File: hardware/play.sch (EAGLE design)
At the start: 12 parts, among them T1 BC547, T2 BC547, T3 BC547, T4 BC547

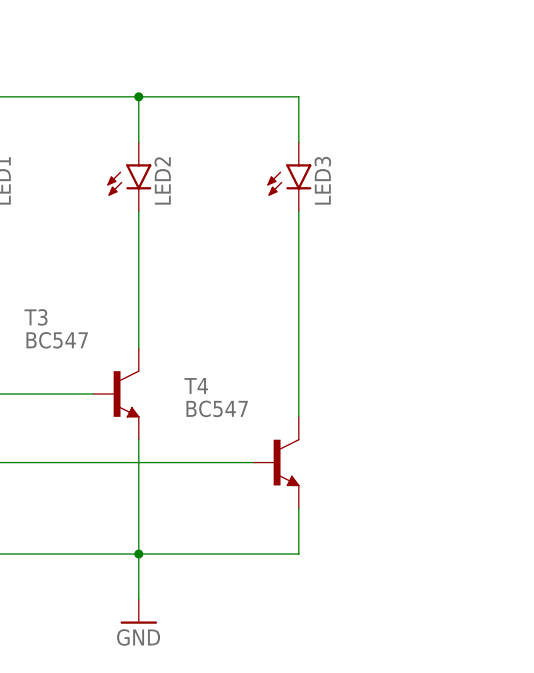
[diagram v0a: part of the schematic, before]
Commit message: Added smoothing cap on the schematic
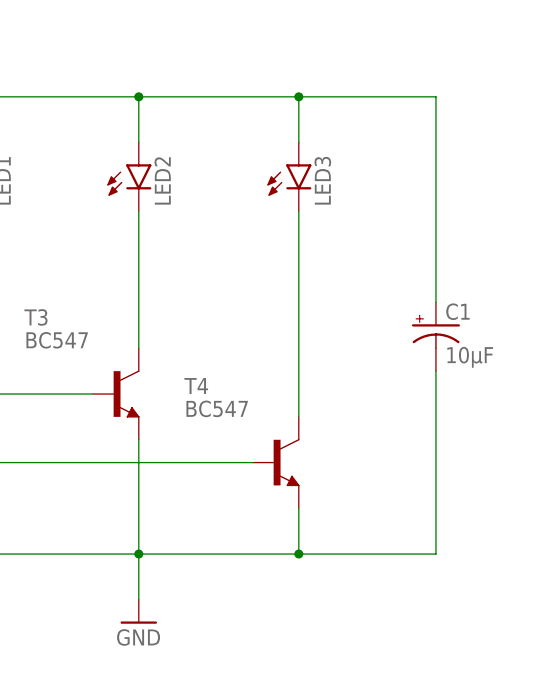
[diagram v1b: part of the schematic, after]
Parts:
- added C1: 10µF, SparkFun-Capacitors:CAP_POLPTH2
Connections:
- net GND: now also C1.-
- net VCC: now also C1.+
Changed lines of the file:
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@@
 <setting verticaltext="up"/>
 </settings>
-<grid distance="0.1" unitdist="inch" unit="inch" style="lines" multiple="1" display="yes" altdistance="0.01" altunitdist="inch" altunit="inch"/>
+<grid distance="0.1" unitdist="inch" unit="inch" style="lines" multiple="1" display="no" altdistance="0.01" altunitdist="inch" altunit="inch"/>
 <layers>
 <layer number="1" name="Top" color="4" fill="1" visible="no" active="no"/>
@@
 </part>
 <part name="S1" library="SparkFun-Electromechanical" deviceset="SWITCH-MOMENTARY-2" device="PTH"/>
+<part name="C1" library="SparkFun-Capacitors" deviceset="CAP_POL" device="PTH2" value="10µF"/>
 </parts>
 <sheets>
@@
 </instance>
 <instance part="S1" gate="G$1" x="68.58" y="33.02" rot="R270"/>
+<instance part="C1" gate="G$1" x="165.1" y="30.48"/>
 </instances>
 <busses>
@@
 <junction x="114.3" y="55.88"/>
 <junction x="132.08" y="55.88"/>
+<pinref part="C1" gate="G$1" pin="+"/>
+<wire x1="149.86" y1="55.88" x2="165.1" y2="55.88" width="0.1524" layer="91"/>
+<wire x1="165.1" y1="55.88" x2="165.1" y2="33.02" width="0.1524" layer="91"/>
+<junction x="149.86" y="55.88"/>
 </segment>
 </net>
@@
 <wire x1="68.58" y1="5.08" x2="114.3" y2="5.08" width="0.1524" layer="91"/>
 <junction x="114.3" y="5.08"/>
+<pinref part="C1" gate="G$1" pin="-"/>
+<wire x1="165.1" y1="25.4" x2="165.1" y2="5.08" width="0.1524" layer="91"/>
+<wire x1="165.1" y1="5.08" x2="149.86" y2="5.08" width="0.1524" layer="91"/>
+<junction x="149.86" y="5.08"/>
 </segment>
 </net>

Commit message: New hardware PCB design, with signal connector
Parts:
- added JP1, JP2: M02PTH, SparkFun-Connectors:M02PTH
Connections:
- net GND: now also JP1.2, JP2.2
- net N$2: now also JP2.1
- net VCC: now also JP1.1
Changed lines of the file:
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@@
 <layer number="111" name="LPC17xx" color="7" fill="1" visible="yes" active="yes"/>
 <layer number="112" name="tSilk" color="7" fill="1" visible="yes" active="yes"/>
+<layer number="113" name="IDFDebug" color="4" fill="1" visible="yes" active="yes"/>
 <layer number="116" name="Patch_BOT" color="9" fill="4" visible="yes" active="yes"/>
 <layer number="121" name="_tsilk" color="7" fill="1" visible="yes" active="yes"/>
@@
 <part name="S1" library="SparkFun-Electromechanical" deviceset="SWITCH-MOMENTARY-2" device="PTH"/>
 <part name="C1" library="SparkFun-Capacitors" deviceset="CAP_POL" device="PTH2" value="10µF"/>
+<part name="JP2" library="SparkFun-Connectors" deviceset="M02" device="PTH"/>
+<part name="JP1" library="SparkFun-Connectors" deviceset="M02" device="PTH"/>
+<part name="SUPPLY3" library="SparkFun-Aesthetics" deviceset="VCC" device=""/>
+<part name="GND3" library="SparkFun-Aesthetics" deviceset="GND" device=""/>
 </parts>
 <sheets>
@@
 <instance part="S1" gate="G$1" x="68.58" y="33.02" rot="R270"/>
 <instance part="C1" gate="G$1" x="165.1" y="30.48"/>
+<instance part="JP2" gate="G$1" x="91.44" y="27.94" rot="R180"/>
+<instance part="JP1" gate="G$1" x="58.42" y="17.78" rot="R180"/>
+<instance part="SUPPLY3" gate="G$1" x="48.26" y="25.4"/>
+<instance part="GND3" gate="1" x="48.26" y="7.62"/>
 </instances>
 <busses>
@@
 <junction x="149.86" y="55.88"/>
 </segment>
+<segment>
+<pinref part="JP1" gate="G$1" pin="1"/>
+<pinref part="SUPPLY3" gate="G$1" pin="VCC"/>
+<wire x1="50.8" y1="17.78" x2="48.26" y2="17.78" width="0.1524" layer="91"/>
+<wire x1="48.26" y1="17.78" x2="48.26" y2="25.4" width="0.1524" layer="91"/>
+</segment>
 </net>
 <net name="GND" class="0">
@@
 <pinref part="S1" gate="G$1" pin="2"/>
 <wire x1="68.58" y1="27.94" x2="68.58" y2="5.08" width="0.1524" layer="91"/>
-<wire x1="68.58" y1="5.08" x2="114.3" y2="5.08" width="0.1524" layer="91"/>
 <junction x="114.3" y="5.08"/>
 <pinref part="C1" gate="G$1" pin="-"/>
+<wire x1="68.58" y1="5.08" x2="83.82" y2="5.08" width="0.1524" layer="91"/>
+<wire x1="83.82" y1="5.08" x2="114.3" y2="5.08" width="0.1524" layer="91"/>
 <wire x1="165.1" y1="25.4" x2="165.1" y2="5.08" width="0.1524" layer="91"/>
 <wire x1="165.1" y1="5.08" x2="149.86" y2="5.08" width="0.1524" layer="91"/>
 <junction x="149.86" y="5.08"/>
+<pinref part="JP2" gate="G$1" pin="2"/>
+<wire x1="83.82" y1="25.4" x2="83.82" y2="5.08" width="0.1524" layer="91"/>
+<junction x="83.82" y="5.08"/>
+</segment>
+<segment>
+<pinref part="GND3" gate="1" pin="GND"/>
+<wire x1="48.26" y1="10.16" x2="48.26" y2="15.24" width="0.1524" layer="91"/>
+<pinref part="JP1" gate="G$1" pin="2"/>
+<wire x1="48.26" y1="15.24" x2="50.8" y2="15.24" width="0.1524" layer="91"/>
 </segment>
 </net>
@@
 <pinref part="R1" gate="G$1" pin="2"/>
 <pinref part="T1" gate="G$1" pin="B"/>
-<wire x1="81.28" y1="43.18" x2="91.44" y2="43.18" width="0.1524" layer="91"/>
-</segment>
-</net>
+<wire x1="81.28" y1="43.18" x2="83.82" y2="43.18" width="0.1524" layer="91"/>
+<pinref part="JP2" gate="G$1" pin="1"/>
+<wire x1="83.82" y1="43.18" x2="91.44" y2="43.18" width="0.1524" layer="91"/>
+<wire x1="83.82" y1="43.18" x2="83.82" y2="27.94" width="0.1524" layer="91"/>
+<junction x="83.82" y="43.18"/>
+</segment>
+</net>

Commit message: Updated hardware
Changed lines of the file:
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@@
 <part name="U$1" library="attiny85" deviceset="ATTINY85" device=""/>
 <part name="SUPPLY1" library="SparkFun-Aesthetics" deviceset="VCC" device=""/>
-<part name="SUPPLY2" library="SparkFun-Aesthetics" deviceset="VCC" device=""/>
 <part name="GND1" library="SparkFun-Aesthetics" deviceset="GND" device=""/>
 <part name="R1" library="SparkFun-Resistors" deviceset="RESISTOR" device="PTH-1/4W" value="1 kΩ">
@@
 <instances>
 <instance part="U$1" gate="G$1" x="38.1" y="40.64"/>
-<instance part="SUPPLY1" gate="G$1" x="66.04" y="58.42"/>
-<instance part="SUPPLY2" gate="G$1" x="66.04" y="58.42"/>
+<instance part="SUPPLY1" gate="G$1" x="66.04" y="63.5"/>
 <instance part="GND1" gate="1" x="38.1" y="33.02"/>
 <instance part="R1" gate="G$1" x="76.2" y="43.18">
@@
 <net name="VCC" class="0">
 <segment>
-<pinref part="SUPPLY1" gate="G$1" pin="VCC"/>
-<pinref part="SUPPLY2" gate="G$1" pin="VCC"/>
-<pinref part="U$1" gate="G$1" pin="VCC"/>
-<wire x1="66.04" y1="50.8" x2="66.04" y2="55.88" width="0.1524" layer="91"/>
+<pinref part="JP1" gate="G$1" pin="1"/>
+<pinref part="SUPPLY3" gate="G$1" pin="VCC"/>
+<wire x1="50.8" y1="17.78" x2="48.26" y2="17.78" width="0.1524" layer="91"/>
+<wire x1="48.26" y1="17.78" x2="48.26" y2="25.4" width="0.1524" layer="91"/>
+</segment>
+<segment>
 <pinref part="U$1" gate="G$1" pin="PB5"/>
-<wire x1="66.04" y1="55.88" x2="66.04" y2="58.42" width="0.1524" layer="91"/>
 <wire x1="38.1" y1="50.8" x2="38.1" y2="55.88" width="0.1524" layer="91"/>
 <wire x1="38.1" y1="55.88" x2="66.04" y2="55.88" width="0.1524" layer="91"/>
-<junction x="66.04" y="55.88"/>
+<pinref part="T1" gate="G$1" pin="C"/>
 <wire x1="66.04" y1="55.88" x2="96.52" y2="55.88" width="0.1524" layer="91"/>
-<pinref part="T1" gate="G$1" pin="C"/>
 <wire x1="96.52" y1="55.88" x2="96.52" y2="48.26" width="0.1524" layer="91"/>
 <wire x1="96.52" y1="55.88" x2="114.3" y2="55.88" width="0.1524" layer="91"/>
@@
 <wire x1="165.1" y1="55.88" x2="165.1" y2="33.02" width="0.1524" layer="91"/>
 <junction x="149.86" y="55.88"/>
-</segment>
-<segment>
-<pinref part="JP1" gate="G$1" pin="1"/>
-<pinref part="SUPPLY3" gate="G$1" pin="VCC"/>
-<wire x1="50.8" y1="17.78" x2="48.26" y2="17.78" width="0.1524" layer="91"/>
-<wire x1="48.26" y1="17.78" x2="48.26" y2="25.4" width="0.1524" layer="91"/>
+<pinref part="U$1" gate="G$1" pin="VCC"/>
+<wire x1="66.04" y1="50.8" x2="66.04" y2="55.88" width="0.1524" layer="91"/>
+<pinref part="SUPPLY1" gate="G$1" pin="VCC"/>
+<wire x1="66.04" y1="55.88" x2="66.04" y2="63.5" width="0.1524" layer="91"/>
+<junction x="66.04" y="55.88"/>
 </segment>
 </net>
